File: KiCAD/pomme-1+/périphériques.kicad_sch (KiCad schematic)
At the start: 23 parts, among them J3 RTS|CTS loop, J4 rs232-socket, J5 rs232-plug, J6 5V MCU UART, J7 DE9_female, Q1 2N3904, U10 MAX232CPE

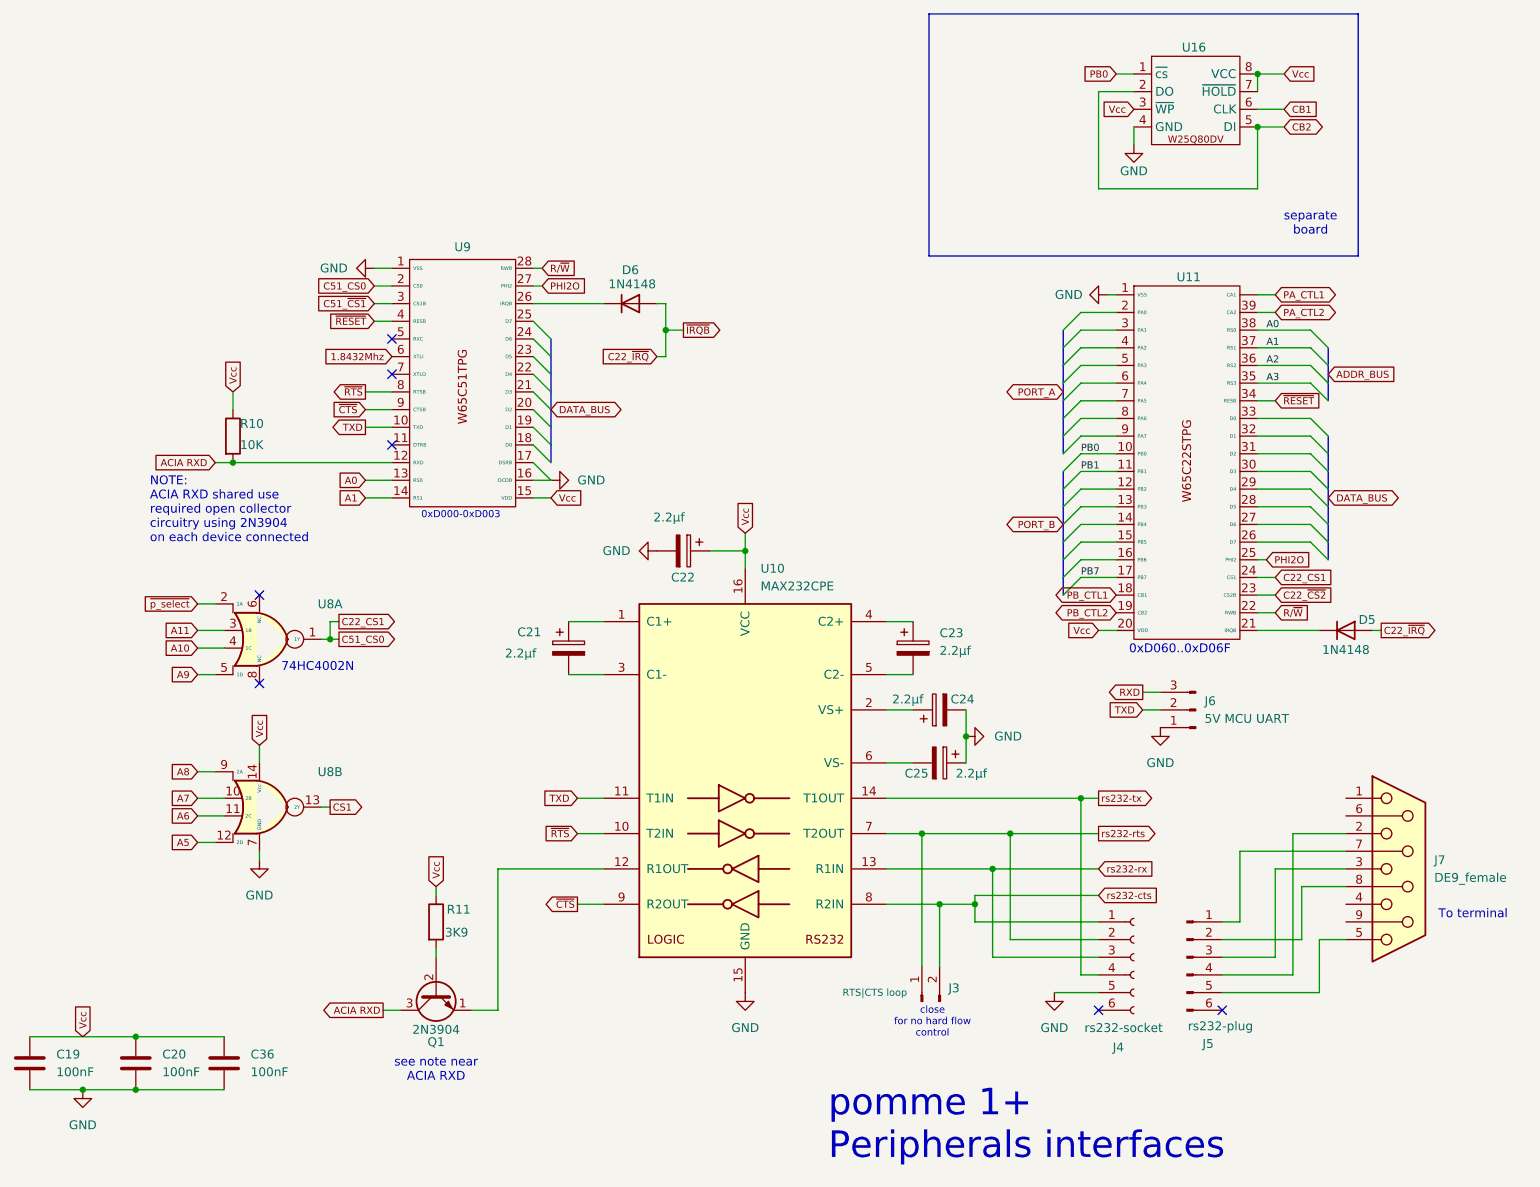
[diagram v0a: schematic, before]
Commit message: Modification du circuit pour ajouter un amplificateur audio LM4861 sur la carte amovible qui se branche sur le connecteur VIA BUS
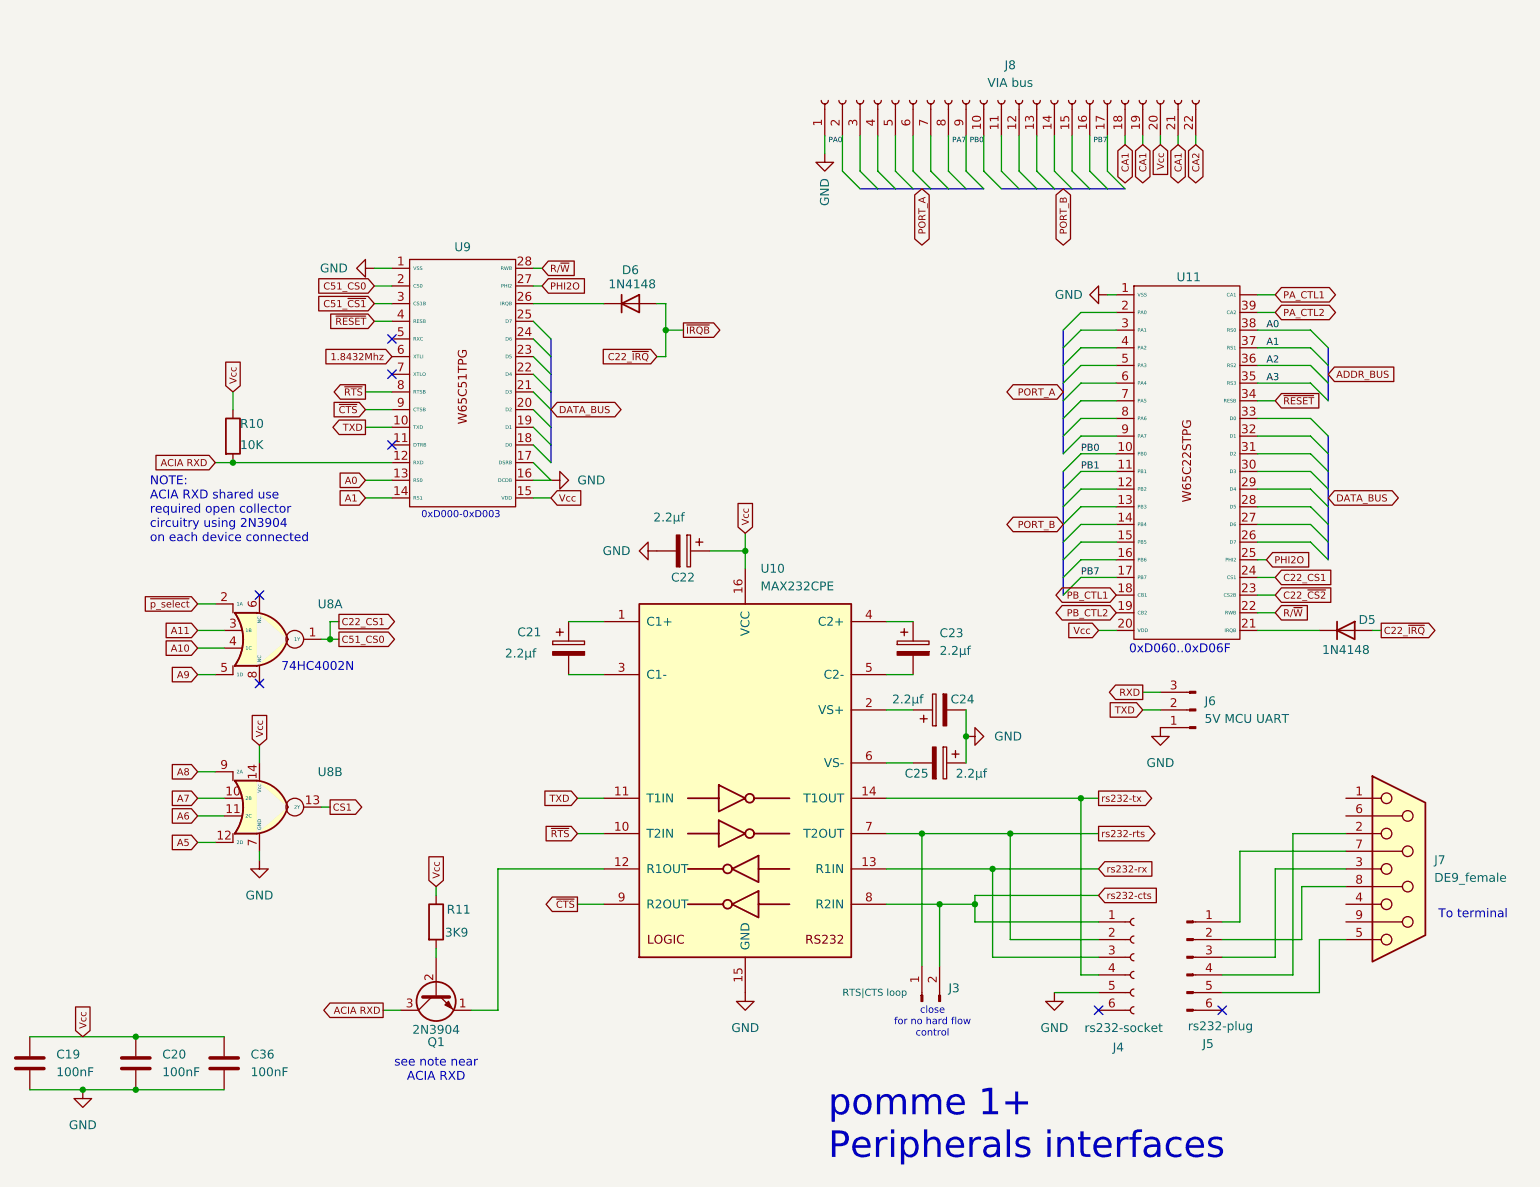
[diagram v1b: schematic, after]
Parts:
- removed U16: ~, symbol W25Q80DV:W25Q80DV
- added J8: VIA bus, symbol Connector:Conn_01x22_Socket
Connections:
- net GND: now also J8.1 (Pin_1)
- net PB0: now also J8.10 (Pin_10)
- net PB7: now also J8.17 (Pin_17)
- net Vcc: now also J8.20 (Pin_20)
- new net CA1: J8.18 (Pin_18), J8.19 (Pin_19), J8.21 (Pin_21)
- new net CA2: J8.22 (Pin_22)
- new net PA0: J8.2 (Pin_2)
- new net PA7: J8.9 (Pin_9)
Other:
- note removed: "separate board"

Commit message: Modification au circuit du pomme-1+ ajout d'une seconde EEPROM (U13) 0xC000...0xDFFF. Celle-ci peut-être programmée dans le circuit.
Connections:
- net U13_~{BUSY}: now reaches U11.12 (PB2)
- net PB1 renamed U13_~{WE}
- no-connect marks 7 -> 9
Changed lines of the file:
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@@
 	)
 	(junction
+		(at 214.63 80.01)
+		(diameter 0)
+		(color 0 0 0 0)
+	)
+	(junction
 		(at 214.63 127)
 		(diameter 0)
@@
 	)
 	(junction
+		(at 214.63 82.55)
+		(diameter 0)
+		(color 0 0 0 0)
+	)
+	(junction
 		(at 166.37 91.44)
 		(diameter 0)
@@
 	)
 	(no_connect
+		(at 203.2 26.67)
+	)
+	(no_connect
 		(at 234.95 157.48)
 	)
@@
 	)
 	(no_connect
+		(at 205.74 26.67)
+	)
+	(no_connect
 		(at 217.17 157.48)
 	)
@@
 	(wire
 		(pts
+			(xy 212.09 80.01) (xy 214.63 80.01)
+		)
+		(stroke
+			(width 0)
+			(type default)
+		)
+	)
+	(wire
+		(pts
 			(xy 154.94 59.69) (xy 157.48 59.69)
 		)
@@
 		)
 	)
+	(wire
+		(pts
+			(xy 207.01 82.55) (xy 212.09 82.55)
+		)
+		(stroke
+			(width 0)
+			(type default)
+		)
+	)
 	(bus
 		(pts
@@
 	(wire
 		(pts
+			(xy 207.01 80.01) (xy 212.09 80.01)
+		)
+		(stroke
+			(width 0)
+			(type default)
+		)
+	)
+	(wire
+		(pts
 			(xy 187.96 31.75) (xy 187.96 36.83)
 		)
@@
 	(wire
 		(pts
+			(xy 212.09 82.55) (xy 214.63 82.55)
+		)
+		(stroke
+			(width 0)
+			(type default)
+		)
+	)
+	(wire
+		(pts
 			(xy 223.52 31.75) (xy 223.52 33.02)
 		)
@@
 		)
 	)
+	(label "PB2"
+		(at 214.63 82.55 0)
+		(effects
+			(font
+				(size 1.016 1.016)
+			)
+			(justify left bottom)
+		)
+	)
 	(label "PB1"
 		(at 214.63 80.01 0)
@@
 		)
 	)
+	(global_label "U13_~{WE}"
+		(shape output)
+		(at 207.01 80.01 180)
+		(fields_autoplaced yes)
+		(effects
+			(font
+				(size 1.27 1.27)
+			)
+			(justify right)
+		)
+		(property "Intersheetrefs" "${INTERSHEET_REFS}"
+			(at 196.7073 80.01 0)
+			(effects
+				(font
+					(size 1.27 1.27)
+				)
+				(justify right)
+				(hide yes)
+			)
+		)
+	)
 	(global_label "Vcc"
 		(shape input)
@@
 			(effects
 				(font
+					(size 1.27 1.27)
+				)
+				(justify right)
+				(hide yes)
+			)
+		)
+	)
+	(global_label "U13_~{BUSY}"
+		(shape input)
+		(at 207.01 82.55 180)
+		(fields_autoplaced yes)
+		(effects
+			(font
+				(size 1.27 1.27)
+			)
+			(justify right)
+		)
+		(property "Intersheetrefs" "${INTERSHEET_REFS}"
+			(at 194.4091 82.55 0)
+			(effects
+				(font

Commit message: Modification au circuit pour supprimer le polling de la pin 1 de U13, car ça ne fonctionne pas bien. La solution logiciel est plus fiable.
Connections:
- net PA0: now also U11.2 (PA0)
- net PA7: now also U11.9 (PA7)
- net PB3: now reaches U11.13 (PB3)
- net PB4: now reaches U11.14 (PB4)
- net PB5: now reaches U11.15 (PB5)
- net PB6: now reaches U11.16 (PB6)
- net PA1: now reaches U11.3 (PA1)
- net PA2: now reaches U11.4 (PA2)
- net PA3: now reaches U11.5 (PA3)
- net PA4: now reaches U11.6 (PA4)
- net PA5: now reaches U11.7 (PA5)
- net PA6: now reaches U11.8 (PA6)
- net U13_~{BUSY} renamed PB2
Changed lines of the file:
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@@
 	)
 	(junction
-		(at 214.63 82.55)
-		(diameter 0)
-		(color 0 0 0 0)
-	)
-	(junction
 		(at 166.37 91.44)
 		(diameter 0)
@@
 		)
 	)
-	(wire
-		(pts
-			(xy 207.01 82.55) (xy 212.09 82.55)
-		)
-		(stroke
-			(width 0)
-			(type default)
-		)
-	)
 	(bus
 		(pts
@@
 	(wire
 		(pts
-			(xy 212.09 82.55) (xy 214.63 82.55)
-		)
-		(stroke
-			(width 0)
-			(type default)
-		)
-	)
-	(wire
-		(pts
 			(xy 223.52 31.75) (xy 223.52 33.02)
 		)
@@
 		)
 	)
+	(label "PB4"
+		(at 214.63 87.63 0)
+		(effects
+			(font
+				(size 1.016 1.016)
+			)
+			(justify left bottom)
+		)
+	)
+	(label "PA3"
+		(at 214.63 64.77 0)
+		(effects
+			(font
+				(size 1.016 1.016)
+			)
+			(justify left bottom)
+		)
+	)
 	(label "PB0"
 		(at 214.63 77.47 0)
@@
 		)
 	)
+	(label "PA0"
+		(at 214.63 57.15 0)
+		(effects
+			(font
+				(size 1.016 1.016)
+			)
+			(justify left bottom)
+		)
+	)
+	(label "PA6"
+		(at 214.63 72.39 0)
+		(effects
+			(font
+				(size 1.016 1.016)
+			)
+			(justify left bottom)
+		)
+	)
 	(label "A2"
 		(at 241.3 64.77 0)
@@
 		)
 	)
+	(label "PA5"
+		(at 214.63 69.85 0)
+		(effects
+			(font
+				(size 1.016 1.016)
+			)
+			(justify left bottom)
+		)
+	)
 	(label "PA0"
 		(at 180.34 33.02 180)
@@
 		)
 	)
+	(label "PB3"
+		(at 214.63 85.09 0)
+		(effects
+			(font
+				(size 1.016 1.016)
+			)
+			(justify left bottom)
+		)
+	)
+	(label "PA2"
+		(at 214.63 62.23 0)
+		(effects
+			(font
+				(size 1.016 1.016)
+			)
+			(justify left bottom)
+		)
+	)
+	(label "PB6"
+		(at 214.63 92.71 0)
+		(effects
+			(font
+				(size 1.016 1.016)
+			)
+			(justify left bottom)
+		)
+	)
+	(label "PA7"
+		(at 214.63 74.93 0)
+		(effects
+			(font
+				(size 1.016 1.016)
+			)
+			(justify left bottom)
+		)
+	)
 	(label "PB7"
 		(at 218.44 33.02 180)
@@
 		)
 	)
+	(label "PB5"
+		(at 214.63 90.17 0)
+		(effects
+			(font
+				(size 1.016 1.016)
+			)
+			(justify left bottom)
+		)
+	)
+	(label "PA4"
+		(at 214.63 67.31 0)
+		(effects
+			(font
+				(size 1.016 1.016)
+			)
+			(justify left bottom)
+		)
+	)
 	(label "PA7"
 		(at 198.12 33.02 180)
@@
 		)
 	)
+	(label "PA1"
+		(at 214.63 59.69 0)
+		(effects
+			(font
+				(size 1.016 1.016)
+			)
+			(justify left bottom)
+		)
+	)
 	(global_label "TXD"
 		(shape input)
@@
 			(effects
 				(font
-					(size 1.27 1.27)
-				)
-				(justify right)
-				(hide yes)
-			)
-		)
-	)
-	(global_label "U13_~{BUSY}"
-		(shape input)
-		(at 207.01 82.55 180)
-		(fields_autoplaced yes)
-		(effects
-			(font
-				(size 1.27 1.27)
-			)
-			(justify right)
-		)
-		(property "Intersheetrefs" "${INTERSHEET_REFS}"
-			(at 194.4091 82.55 0)
-			(effects
-				(font
